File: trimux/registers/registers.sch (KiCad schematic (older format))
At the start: 33 parts, among them P1 CONN_02X05, U1 trimux, U2 trimux, U3 trimux, U4 trimux, U5 trimux, U6 trimux

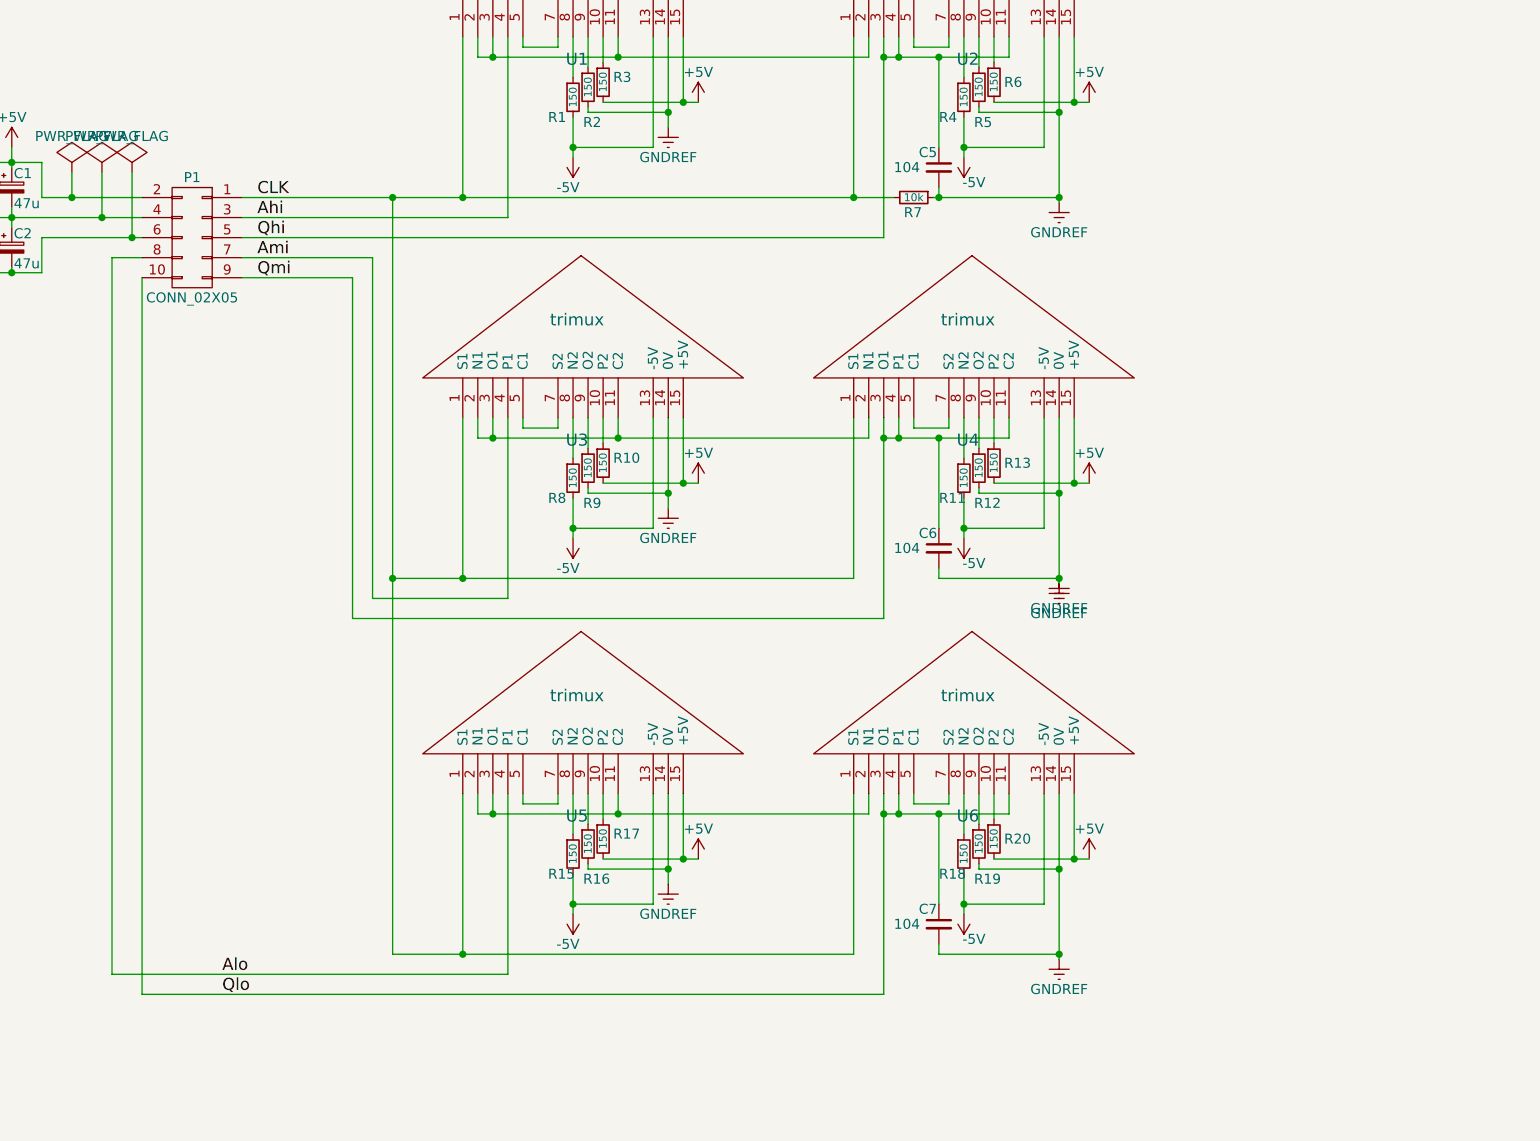
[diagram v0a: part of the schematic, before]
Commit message: leds for the flipflapflop register
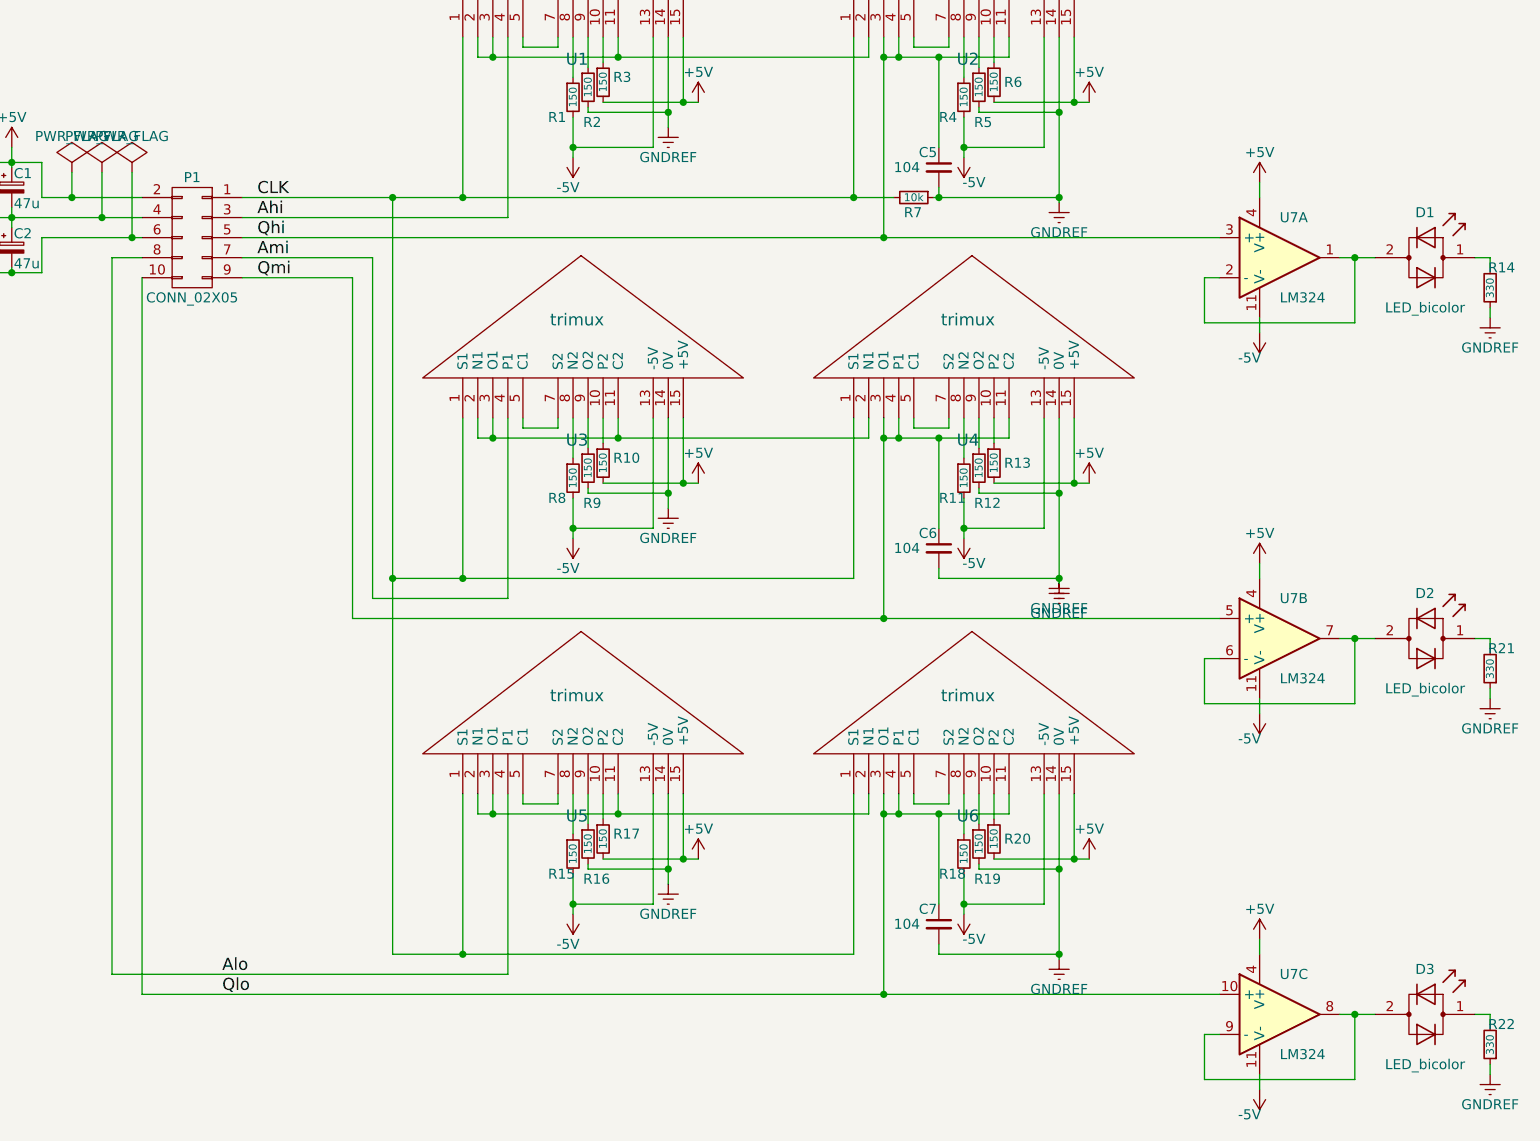
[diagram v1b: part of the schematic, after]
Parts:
- added D1, D2, D3: LED_bicolor, LEDs:LED_D5.0mm, symbol LED_bicolor
- added R14, R21, R22: 330, Resistors_SMD:R_1206_HandSoldering, symbol R_Small
- added U7: LM324, SMD_Packages:SOIC-14_N, symbol LM324
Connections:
- net +5V: now also U7.4 (V+), U7.4 (V+), U7.4 (V+)
- net -5V: now also U7.11 (V-), U7.11 (V-), U7.11 (V-)
- net GNDREF: now also R14.1, R21.1, R22.1
- net Qhi: now also U7.3 (+)
- net Qlo: now also U7.10 (+)
- net Qmi: now also U7.5 (+)
- new net: D1.2 (AK), U7.1, U7.2 (-)
- new net: D1.1 (KA), R14.2
- new net: D2.2 (AK), U7.6 (-), U7.7
- new net: D2.1 (KA), R21.2
- new net: D3.2 (AK), U7.8, U7.9 (-)
- new net: D3.1 (KA), R22.2

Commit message: adapter board final routing
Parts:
- added C10, C11: 47u, Capacitors_THT:CP_Radial_D5.0mm_P2.50mm, symbol CP_Small
- added C8, C9: 104, Capacitors_SMD:C_1206_HandSoldering, symbol C_Small
- added P2: CONN_02X08, symbol CONN_02X08
- added R23, R24, R25: 150, Resistors_SMD:R_1206_HandSoldering, symbol R_Small
- added U10, U12, U8, U9: trimux, trimux:trimux1x15_2.54, symbol trimux
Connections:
- net +5V: now also C10.1, C8.1, P2.14 (P14), R25.2, U10.15 (+5V), U12.15 (+5V), U8.15 (+5V), U9.15 (+5V)
- net -5V: now also C11.2, C9.2, P2.16 (P16), R23.2, U10.13 (-5V), U12.13 (-5V), U8.13 (-5V), U9.13 (-5V)
- net GNDREF: now also C10.2, C11.1, C8.2, C9.1, P2.15 (P15), R24.2, U10.14 (0V), U12.14 (0V), U8.14 (0V), U9.14 (0V)
- new net: R25.1, U12.10 (P2)
- new net: U12.5 (C1), U12.7 (S2)
- new net: R23.1, U12.8 (N2)
- new net: R24.1, U12.9 (O2)

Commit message: memory
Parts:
- added P3: CONN_01X04, Pin_Headers:Pin_Header_Straight_1x04_Pitch2.54mm, symbol CONN_01X04
- C1, C10, C11, C2: footprint Capacitors_THT:CP_Radial_D5.0mm_P2.50mm -> Capacitors_THT:CP_Radial_D5.0mm_P2.00mm
- P2: footprint (none) -> registers:IDC16
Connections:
- net at P2.1 (P1): now also U10.2 (N1), U10.3 (O1)
- net at P2.10 (P10): now also U9.4 (P1)
- net at P2.11 (P11): now also U9.8 (N2)
- net at P2.12 (P12): now also U9.9 (O2)
- net at P2.13 (P13): now also U9.10 (P2)
- net at P2.2 (P2): now also U8.2 (N1)
- net at P2.3 (P3): now also U8.3 (O1)
- net at P2.4 (P4): now also U8.4 (P1)
- net at P2.5 (P5): now also U8.8 (N2)
- net at P2.6 (P6): now also U8.9 (O2)
- net at P2.7 (P7): now also U8.10 (P2)
- net at P2.8 (P8): now also U9.2 (N1)
- net at P2.9 (P9): now also U9.3 (O1)
- net HI: now reaches U12.1 (S1)
- net HI: now also P3.3 (P3)
- net C/A/Q: now reaches U12.11 (C2)
- net C/A/Q: now also P3.4 (P4)
- net at U12.2 (N1): now also U10.5 (C1), U12.3 (O1)
- net at U12.4 (P1): now also U10.11 (C2)
- net MI: now reaches U10.1 (S1)
- net MI: now also U10.7 (S2), P3.2 (P2)
- net at U10.10 (P2): now also U9.11 (C2)
- net at U10.4 (P1): now also U8.5 (C1)
- net at U10.8 (N2): now also U8.11 (C2)
- net at U10.9 (O2): now also U9.5 (C1)
- net LO: now reaches U8.1 (S1)
- net LO: now also U8.7 (S2), U9.1 (S1), U9.7 (S2), P3.1 (P1)
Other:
- moved on the sheet: C10, C11, C8, C9, P2, R23, R24, R25, U10, U12, U8, U9

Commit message: memory
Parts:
- added C12, C13, C14, C15, C16, C19, C20: 104, Capacitors_SMD:C_1206_HandSoldering, symbol C_Small
- added C17, C18: 47u, Capacitors_THT:CP_Radial_D5.0mm_P2.00mm, symbol CP_Small
- added D4, D5, D6: LED_bicolor, LEDs:LED_D5.0mm, symbol LED_bicolor
- added J1: Conn_01x01, Pin_Headers:Pin_Header_Straight_1x01_Pitch2.54mm, symbol Conn_01x01
- added P4: CONN_02X05, registers:IDC10, symbol CONN_02X05
- added R26, R27, R28, R29, R31, R32, R33: 150, Resistors_SMD:R_1206_HandSoldering, symbol R_Small
- added R30: 10k, Resistors_SMD:R_1206_HandSoldering, symbol R_Small
- added R34, R35, R36: 330, Resistors_SMD:R_1206_HandSoldering, symbol R_Small
- added U11, U13, U14: trimux, trimux:trimux1x15_2.54, symbol trimux
- added U15: LM324, SMD_Packages:SOIC-14_N, symbol LM324
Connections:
- net +5V: now also C15.1, C17.1, P4.2 (P2), R28.2, R33.2, U11.15 (+5V), U13.15 (+5V), U14.15 (+5V), U15.4 (V+), U15.4 (V+), U15.4 (V+)
- net -5V: now also C16.2, C18.2, P4.6 (P6), R26.2, R29.2, R31.2, U11.13 (-5V), U13.13 (-5V), U14.13 (-5V), U15.11 (V-), U15.11 (V-), U15.11 (V-)
- net Ahi: now also P4.3 (P3), U11.4 (P1)
- net Alo: now also P4.8 (P8)
- net Ami: now also P4.7 (P7)
- net CLK: now also P4.1 (P1), R30.2, U11.1 (S1), U14.1 (S1)
- net GNDREF: now also C12.2, C13.2, C14.2, C15.2, C16.1, C17.2, C18.1, C19.2, C20.2, P4.4 (P4), R27.2, R30.1, R32.2, R34.1, R35.1, R36.1, U11.14 (0V), U13.14 (0V), U14.14 (0V)
- net Qhi: now also C20.1, P4.5 (P5), U13.11 (C2), U14.3 (O1), U14.4 (P1), U15.5 (+)
- net Qlo: now also P4.10 (P10), U15.3 (+)
- net Qmi: now also P4.9 (P9), U15.10 (+)
- net at U1.11 (C2), U1.2 (N1), U1.3 (O1)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: now also C12.1
- net at U3.11 (C2), U3.2 (N1), U3.3 (O1)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: now also C13.1
- net at U5.11 (C2), U5.2 (N1), U5.3 (O1)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: now also C14.1
- new net: R28.1, U11.10 (P2)
- new net: U11.11 (C2), U13.2 (N1)
- new net: C19.1, U11.2 (N1), U11.3 (O1), U13.5 (C1), U14.2 (N1)
- new net: U11.5 (C1), U11.7 (S2)
- new net: R26.1, U11.8 (N2)
- new net: R27.1, U11.9 (O2)
- new net: R33.1, U14.10 (P2)
- new net: U13.8 (N2), U14.11 (C2)
- new net: U14.5 (C1), U14.7 (S2)
- new net: R31.1, U14.8 (N2)
- new net: R32.1, U14.9 (O2)
- new net: D6.2 (AK), U15.6 (-), U15.7
- new net: D6.1 (KA), R36.2
- new net: R29.1, U13.10 (P2), U13.3 (O1), U13.4 (P1), U13.9 (O2)
- new net: D4.2 (AK), U15.8, U15.9 (-)
- new net: D4.1 (KA), R34.2
- new net: D5.2 (AK), U15.1, U15.2 (-)
- new net: D5.1 (KA), R35.2
- new net RESET: J1.1 (Pin_1), U13.1 (S1), U13.7 (S2)

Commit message: memory board
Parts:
- removed C15, C16, C19, C20: 104, Capacitors_SMD:C_1206_HandSoldering, symbol C_Small
- removed C17, C18: 47u, Capacitors_THT:CP_Radial_D5.0mm_P2.00mm, symbol CP_Small
- removed D4, D5, D6: LED_bicolor, LEDs:LED_D5.0mm, symbol LED_bicolor
- removed J1: Conn_01x01, Pin_Headers:Pin_Header_Straight_1x01_Pitch2.54mm, symbol Conn_01x01
- removed P4: CONN_02X05, registers:IDC10, symbol CONN_02X05
- removed R26, R27, R28, R29, R31, R32, R33: 150, Resistors_SMD:R_1206_HandSoldering, symbol R_Small
- removed R30: 10k, Resistors_SMD:R_1206_HandSoldering, symbol R_Small
- removed R34, R35, R36: 330, Resistors_SMD:R_1206_HandSoldering, symbol R_Small
- removed U11, U13, U14: trimux, trimux:trimux1x15_2.54, symbol trimux
- removed U15: LM324, SMD_Packages:SOIC-14_N, symbol LM324
- added P4, P5, P6, P7, P8, P9: CONN_01X02, Pin_Headers:Pin_Header_Straight_1x02_Pitch1.27mm, symbol CONN_01X02
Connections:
- net Qhi: now also P5.2 (P2); no longer U2.11 (C2)
- net Qlo: now also P9.2 (P2); no longer U6.11 (C2)
- net Qmi: now also P8.2 (P2); no longer U4.11 (C2)
- net at C12.1, U1.2 (N1), U1.3 (O1)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: now also P4.2 (P2); no longer U1.11 (C2)
- net at C13.1, U3.2 (N1), U3.3 (O1)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: now also P6.2 (P2); no longer U3.11 (C2)
- net at C14.1, U5.2 (N1), U5.3 (O1)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: now also P7.2 (P2); no longer U5.11 (C2)
- new net: P4.1 (P1), U1.11 (C2)
- new net: P6.1 (P1), U3.11 (C2)
- new net: P8.1 (P1), U4.11 (C2)
- new net: P5.1 (P1), U2.11 (C2)
- new net: P7.1 (P1), U5.11 (C2)
- new net: P9.1 (P1), U6.11 (C2)
